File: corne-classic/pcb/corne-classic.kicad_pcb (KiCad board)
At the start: 2 copper layers, 152.8 x 92.2 mm, 89 parts, among them J1 MJ-4PP-9, J2 OLED, J3 LED, P1 i2c-pin, P2 i2c-pin, SW1 SW_PUSH, SW10 SW_PUSH, SW11 SW_PUSH, SW12 SW_PUSH, SW13 SW_PUSH, SW14 SW_PUSH, SW15 SW_PUSH, SW16 SW_PUSH, SW17 SW_PUSH, SW18 SW_PUSH, SW19 SW_PUSH, SW2 SW_PUSH, SW20 SW_PUSH, SW21 SW_PUSH, SW22 SW_PUSH, SW3 SW_PUSH, SW4 SW_PUSH, SW5 SW_PUSH, SW6 SW_PUSH, SW7 SW_PUSH, SW8 SW_PUSH, SW9 SW_PUSH, U1 ProMicro

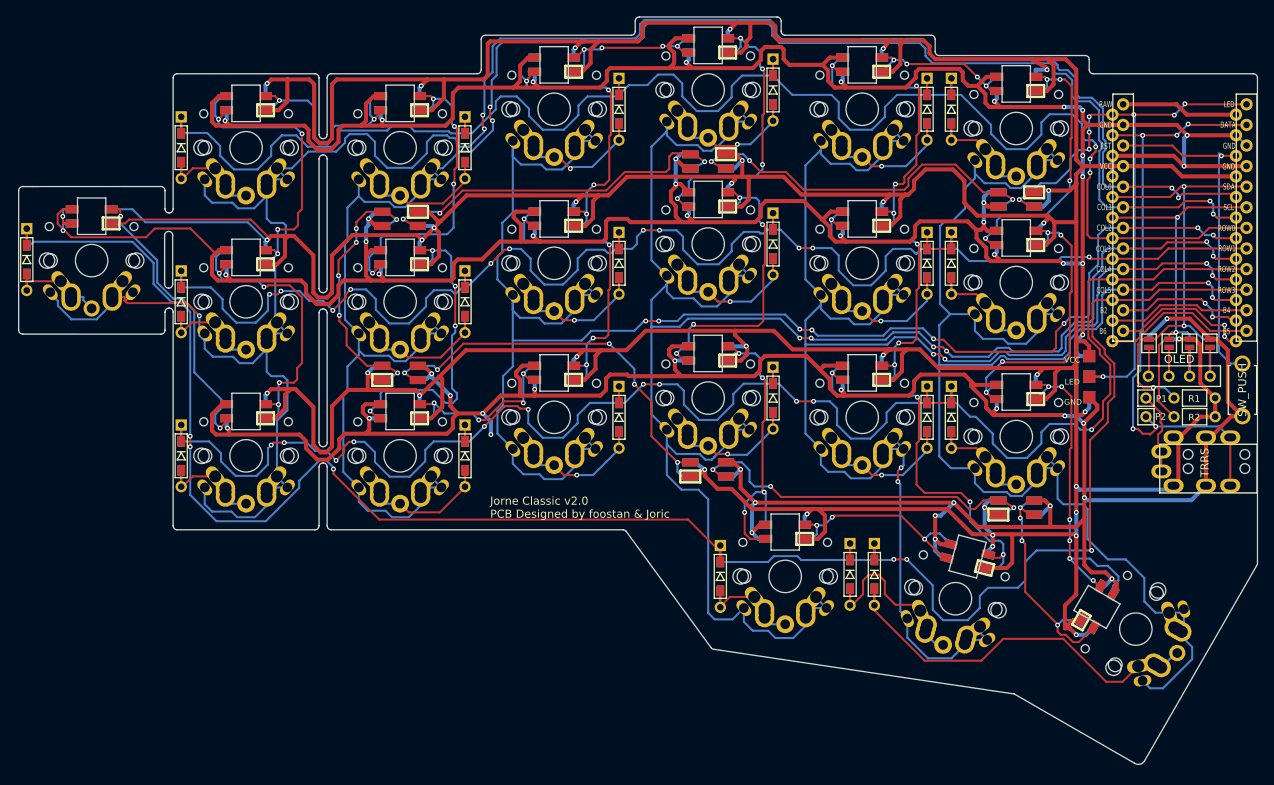
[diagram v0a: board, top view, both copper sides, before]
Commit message: added zones, fixed silk
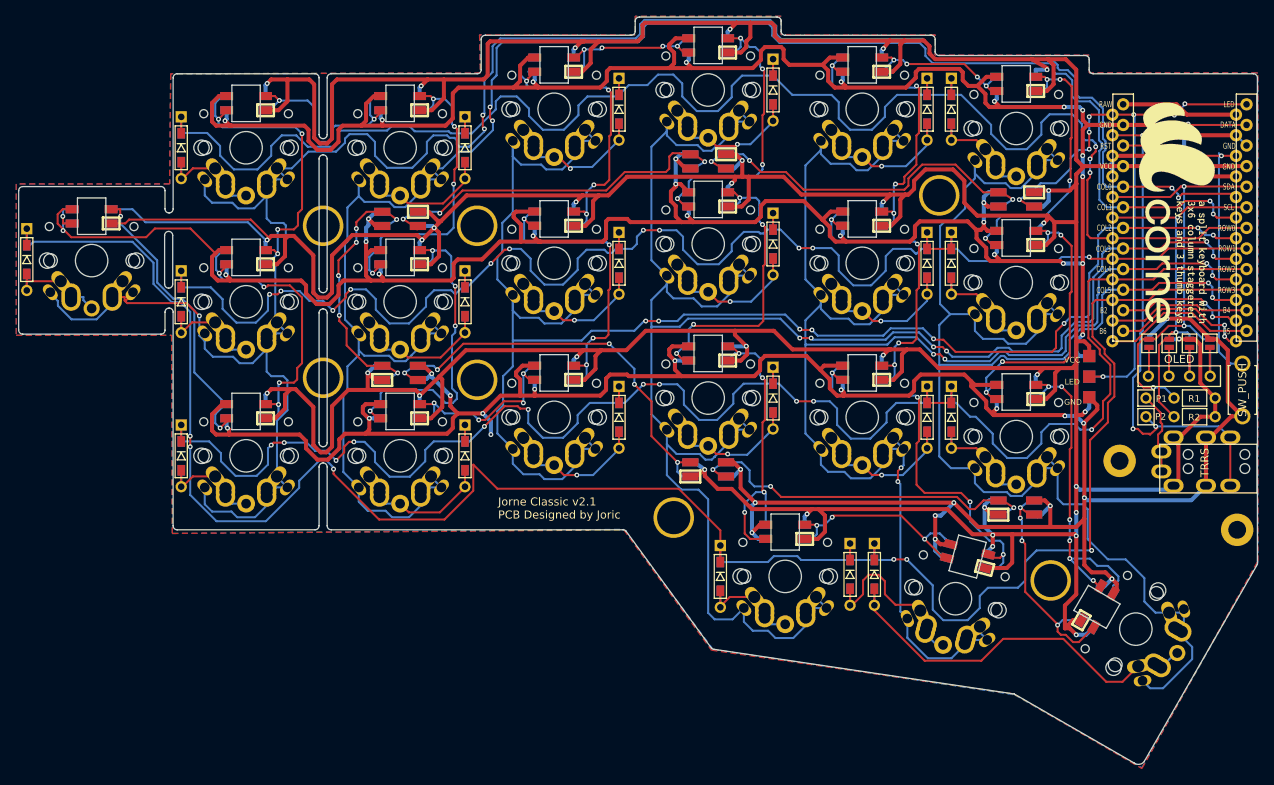
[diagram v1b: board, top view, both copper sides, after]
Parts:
- added ?: , kbd:LEGO_HOLE, F.Cu at (79.5, 105.5)
- added ?: , kbd:LEGO_HOLE, F.Cu at (177.8, 115.8)
- added ?: , kbd:LEGO_HOLE, F.Cu at (192.2, 124.2)
- added ?: , kbd:LEGO_HOLE, F.Cu at (79.5, 86.8)
- added ?: , kbd:LEGO_HOLE, F.Cu at (98.5, 86.8)
- added ?: , kbd:LEGO_HOLE, F.Cu at (98.5, 105.8)
- added ?: , kbd:LEGO_HOLE, F.Cu at (155.5, 83.0)
- added ?: , kbd:LEGO_HOLE, F.Cu at (122.8, 122.8)
- added ?: , kbd:LEGO_HOLE, F.Cu at (169.2, 130.5)
- added G***: LOGO, kbd:corne, B.Cu at (184.0, 85.0)
- added G***: LOGO, kbd:corne, F.Cu at (184.7, 85.2)
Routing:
- net row3: track 249.7 -> 257.9 mm
- added copper zone on B.Cu, net GND
- added copper zone on F.Cu, net GND
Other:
- board text added: "Jorne Classic v2.1 PCB Designed by Joric"
- board text removed: "Jorne Classic v2.0 PCB Designed by foostan & Joric"

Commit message: fixed schematic
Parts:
- G1, G2: renamed from G***; value LOGO -> Logo_Open_Hardware_Small
- H1, H2, H3, H4, H5, H6, H7, H8, H9: renamed from ?; value (none) -> MountingHole
- L1, L2, L3, L4, L5, L6: footprint kbd:SK6812MINI_underglow_rev -> kbd:SK6812MINI_underglow
